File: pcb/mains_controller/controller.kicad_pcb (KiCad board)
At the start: 2 copper layers, 60 x 70 mm, 39 parts, among them J1 Conn_01x03, J2 Conn_01x03, J3 RELAY_CONN, J4 Remote_header, J5 PWR_IN, J6 MFRC_CONN, J7 Micro_SD_Card, J8 Conn_01x03, J9 Conn_01x03, Q1 MMBT3906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

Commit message: Start design for mains controller
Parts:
- removed J3: RELAY_CONN, TerminalBlock_MetzConnect:TerminalBlock_MetzConnect_Type059_RT06302HBWC_1x02_P3.50mm_Horizontal
- removed J4: Remote_header, TerminalBlock_MetzConnect:TerminalBlock_MetzConnect_Type059_RT06304HBWC_1x04_P3.50mm_Horizontal
- removed J5: PWR_IN, TerminalBlock_MetzConnect:TerminalBlock_MetzConnect_Type059_RT06302HBWC_1x02_P3.50mm_Horizontal
- removed JP1: RELAY_VOLT_SELECT, Jumper:SolderJumper-3_P1.3mm_Open_Pad1.0x1.5mm
- removed JP2, JP3: Jumper_2_Open, Jumper:SolderJumper-2_P1.3mm_Open_Pad1.0x1.5mm
- removed Q1, Q2: MMBT3906, Package_TO_SOT_SMD:SOT-23
- removed R1: 5R1, Resistor_SMD:R_1210_3225Metric_Pad1.30x2.65mm_HandSolder
- removed R2: 470R, Resistor_SMD:R_1210_3225Metric_Pad1.30x2.65mm_HandSolder
- removed R8: R10K, Resistor_SMD:R_1210_3225Metric_Pad1.30x2.65mm_HandSolder
- removed U1: ~, RS485_to_ttl:RS485_to_ttl
- removed U2: ~, DC-DC:hw-1338
- added PS1: HLK-PM01, Converter_ACDC:Converter_ACDC_Hi-Link_HLK-PMxx, F.Cu at (53.0, 92.3)
- moved J9 42.5 mm to (35.1, 67.8)
- moved J8 25.8 mm to (35.1, 58.4)
- moved D1 11.5 mm to (59.9, 64.9)
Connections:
- A1 pad 39: +5V -> RELAY+
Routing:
- net +5V: track 110.2 -> 0.00 mm, vias 4 -> 0
- net +3V3: track 208.8 -> 120.9 mm
- net GPIO_ACC4: track 91.6 -> 13.2 mm
- net +VDC: track 55.6 -> 0.00 mm, vias 1 -> 0
- net RS485_RX: track 55.6 -> 15.8 mm
- net GPIO_ACC3: track 45.0 -> 6.91 mm
- net RS485_TX: track 58.8 -> 23.9 mm
- net RELAY-: track 34.6 -> 6.30 mm
- net REMOTE_PWR: track 22.4 -> 0.00 mm, vias 1 -> 0
- net Net-(Q1-B): track 14.2 -> 0.00 mm
- net RELAY+: track 37.9 -> 23.8 mm, vias 0 -> 1
- net GPIO_ACC1: track 66.1 -> 52.1 mm
- net A+: track 10.6 -> 0.00 mm
- net B-: track 10.3 -> 0.00 mm
- net Net-(Q1-C): track 9.68 -> 0.00 mm
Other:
- board text added: "GP4"
- board text removed: "+"
- board text removed: "+5V"
- board text removed: "5V"
- board text removed: "A+"
- board text removed: "B-"
- board text removed: "DC IN"
- board text removed: "DC_IN"
- board text removed: "For 3/5V I/P, bridge JP3 For 7-28VDC I/P, install MP1584 module here"
- board text removed: "Optional RS485 module here"
- board text removed: "PSU for remote unit (optional)"
- board text removed: "Pwr via Remote"
- board text removed: "RELAY"
- board text removed: "Relay pwr"

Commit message: Production version (sent to JLC!)
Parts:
- removed J9: Conn_01x03, Connector_JST:JST_XH_B3B-XH-A_1x03_P2.50mm_Vertical
- added F1: Fuse, Fuse:Fuseholder_Clip-5x20mm_Keystone_3517_Inline_P23.11x6.76mm_D1.70mm_Horizontal, F.Cu at (33.3, 112.8)
- added F2: Fuse, Resistor_THT:R_Axial_DIN0204_L3.6mm_D1.6mm_P5.08mm_Horizontal, F.Cu at (72.5, 104.8)
- added J3: Conn_01x03, TerminalBlock_MetzConnect:TerminalBlock_MetzConnect_Type073_RT02603HBLU_1x03_P5.08mm_Horizontal, F.Cu at (47.4, 125.9)
- added J4: Conn_01x04_Pin, Connector_JST:JST_XH_B4B-XH-A_1x04_P2.50mm_Vertical, F.Cu at (36.0, 57.6)
- added J4: Conn_01x03, TerminalBlock_MetzConnect:TerminalBlock_MetzConnect_Type073_RT02603HBLU_1x03_P5.08mm_Horizontal, F.Cu at (65.6, 126.2)
- added J5: Conn_01x02_Pin, Connector_JST:JST_XH_B2B-XH-A_1x02_P2.50mm_Vertical, F.Cu at (85.5, 58.2)
- added K2: Relay_SPDT, Relay_THT:Relay_SPDT_Omron_G2RL-1-E, F.Cu at (80.5, 88.2)
- added R1: 4k7, Resistor_SMD:R_1210_3225Metric_Pad1.30x2.65mm_HandSolder, F.Cu at (42.0, 63.5)
- added R2: 4k7, Resistor_SMD:R_1210_3225Metric_Pad1.30x2.65mm_HandSolder, F.Cu at (46.0, 63.4)
- added RV1: Varistor, Varistor:RV_Disc_D7mm_W4.9mm_P5mm, F.Cu at (75.1, 96.4)
- J8: value Conn_01x03 -> Conn_01x02_Pin; footprint Connector_JST:JST_XH_B3B-XH-A_1x03_P2.50mm_Vertical -> Connector_JST:JST_XH_B2B-XH-A_1x02_P2.50mm_Vertical
- Q3, R3, R7: moved to F.Cu
- moved J8 52.7 mm to (85.5, 73.4)
- moved REF** 45.0 mm to (36.2, 128.2)
- moved REF** 45.0 mm to (86.2, 128.2)
- moved D1 29.5 mm to (84.1, 81.8)
- moved Q3 21.2 mm to (64.4, 78.7)
- moved R3 19.8 mm to (57.9, 80.8), turned to -90 degrees
- moved R7 19.3 mm to (57.9, 75.3)
- moved D4 13.9 mm to (87.9, 64.4), turned to 180 degrees
- moved PS1 13.3 mm to (64.2, 99.5), turned to 180 degrees
- moved D3 8.90 mm to (87.9, 68.3)
- moved R6 8.57 mm to (81.8, 64.4), turned to 0 degrees
- moved R5 6.76 mm to (81.8, 68.3), turned to 0 degrees
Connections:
- A1 pad 1: RS485_TX -> I2C0_SDA
- A1 pad 2: RS485_RX -> I2C0_SCL
- J8 pad 1: +3V3 -> ACCESS_GRANTED
- J8 pad 2: GPIO_ACC3 -> GND
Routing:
- net LINE: track 0.00 -> 129.9 mm
- net NEUT: track 0.00 -> 113.3 mm
- net RELAY+: track 23.8 -> 117.7 mm
- net I2C0_SCL: track 0.00 -> 38.5 mm
- net Net-(F1-Pad2): track 0.00 -> 37.3 mm
- net RELAY-: track 6.30 -> 39.0 mm
- net SW_LINE: track 0.00 -> 30.3 mm
- net I2C0_SDA: track 0.00 -> 26.7 mm
- net Earth: track 0.00 -> 25.1 mm
- net RS485_TX: track 23.9 -> 0.00 mm
- net MOSFET_GATE: track 17.4 -> 36.2 mm, vias 1 -> 2
- net RS485_RX: track 15.8 -> 0.00 mm
- net GPIO_ACC1: track 52.1 -> 66.2 mm, vias 4 -> 2
- net GPIO_ACC4: track 13.2 -> 0.30 mm, vias 1 -> 0
- net +3V3: track 120.9 -> 132.2 mm, vias 2 -> 1
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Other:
- board size 60 x 70 mm -> 60 x 115 mm
- board text added: "+"
- board text added: "+3v3 GND SDA SCL"
- board text added: "Access Control Gen2 240V Controller V1.1"
- board text added: "DENY"
- board text added: "I2C0"
- board text added: "IN"
- board text added: "L N E"
- board text added: "OK"
- board text added: "OUT"
- board text removed: "Access Control Gen2 LowVolt Controller V1.1"
- board text removed: "GP4"
- board text removed: "Relay Mosfet"
- board text removed: "Vin"

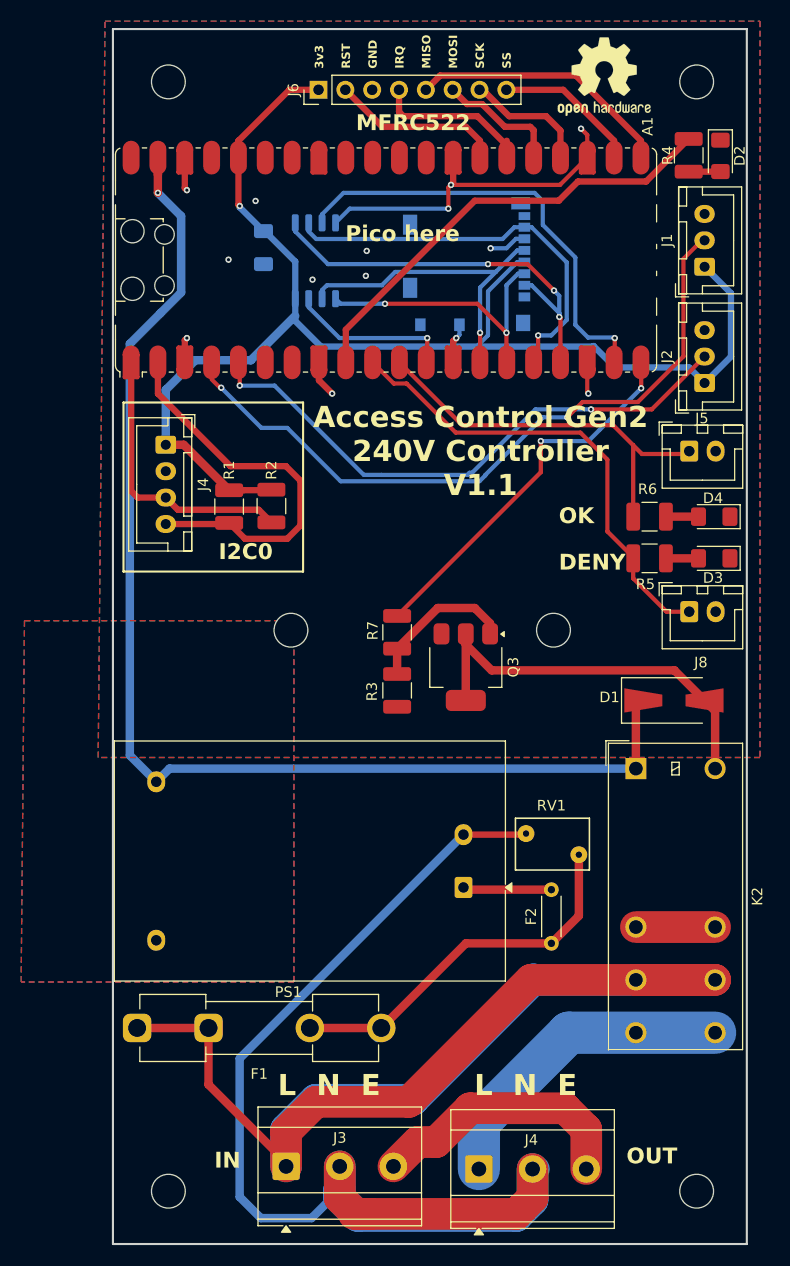
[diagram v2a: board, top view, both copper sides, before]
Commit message: Reposition securing holes for mfrc522 Make hole sizes bigger for varistor and thermal fuse Bump ver to 1.3
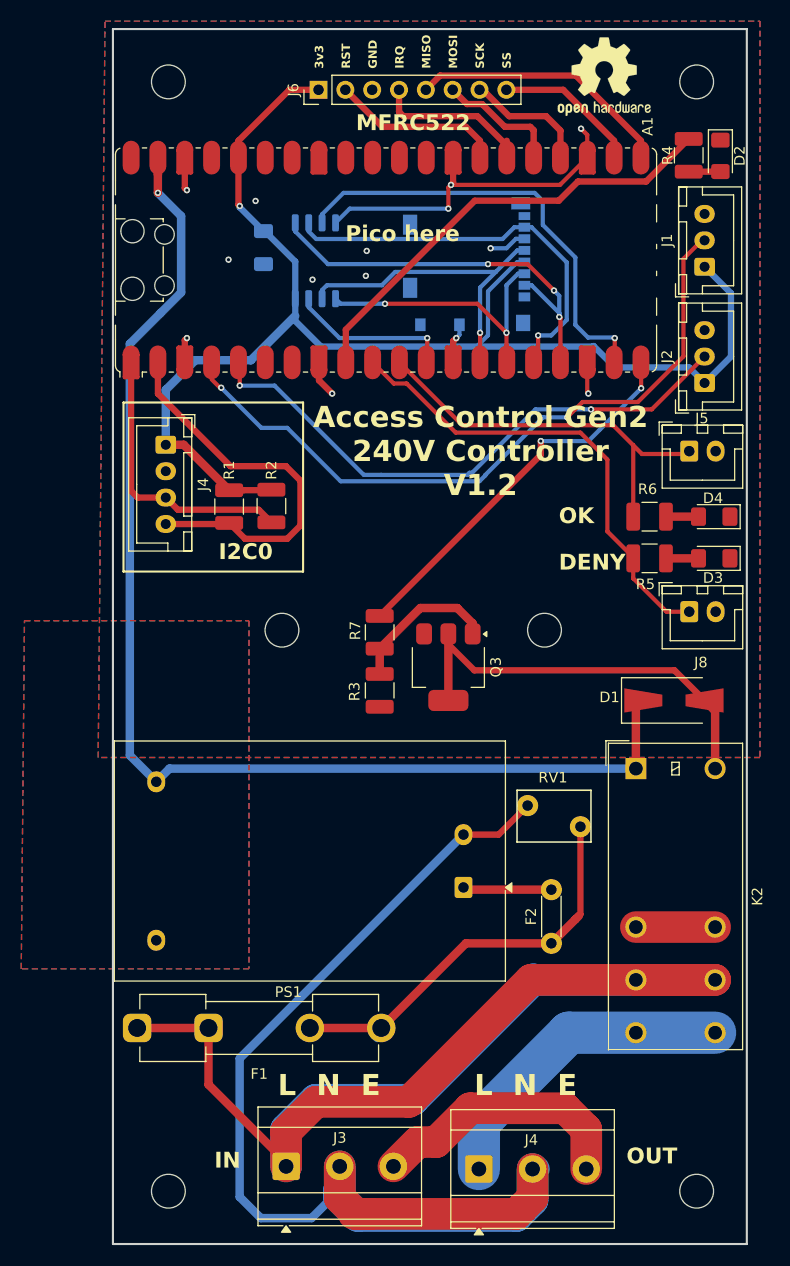
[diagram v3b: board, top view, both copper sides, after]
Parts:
- moved RV1 2.65 mm to (75.2, 93.8)
- moved Q3 1.65 mm to (62.8, 78.7)
- moved R3 1.65 mm to (56.2, 80.8)
- moved R7 1.65 mm to (56.2, 75.3)
- moved REF** 0.85 mm to (71.8, 75.2)
- moved REF** 0.85 mm to (47.0, 75.2)
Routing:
- net Net-(F1-Pad2): track 37.3 -> 40.5 mm
- net RELAY-: track 39.0 -> 40.6 mm
- net NEUT: track 113.3 -> 114.6 mm
- net MOSFET_GATE: track 36.2 -> 36.9 mm
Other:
- board text added: "Access Control Gen2 240V Controller V1.2"
- board text removed: "Access Control Gen2 240V Controller V1.1"
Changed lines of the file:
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@@
 	(footprint "Package_TO_SOT_SMD:SOT-223-3_TabPin2"
 		(layer "F.Cu")
-		(at 64.4 78.65 -90)
+		(at 62.75 78.65 -90)
 		(descr "module CMS SOT223 4 pins")
 		(tags "CMS SOT")
@@
 		(pad "1" thru_hole circle
 			(at 0 0 90)
-			(size 1.4 1.4)
-			(drill 0.7)
+			(size 2 2)
+			(drill 1)
 			(layers "*.Cu" "*.Mask")
 			(remove_unused_layers no)
@@
 		(pad "2" thru_hole circle
 			(at 5.08 0 90)
-			(size 1.4 1.4)
-			(drill 0.7)
+			(size 2 2)
+			(drill 1)
 			(layers "*.Cu" "*.Mask")
 			(remove_unused_layers no)
@@
 	(footprint "Resistor_SMD:R_1210_3225Metric_Pad1.30x2.65mm_HandSolder"
 		(layer "F.Cu")
-		(at 57.9 75.35 -90)
+		(at 56.25 75.35 -90)
 		(descr "Resistor SMD 1210 (3225 Metric), square (rectangular) end terminal, IPC-7351 nominal with elongated pad for handsoldering. (Body size source: IPC-SM-782 page 72, https://www.pcb-3d.com/wordpress/wp-content/uploads/ipc-sm-782a_amendment_1_and_2.pdf), generated with kicad-footprint-generator")
 		(tags "resistor handsolder")
@@
 	(footprint "Resistor_SMD:R_1210_3225Metric_Pad1.30x2.65mm_HandSolder"
 		(layer "F.Cu")
-		(at 57.9 80.85 -90)
+		(at 56.25 80.85 -90)
 		(descr "Resistor SMD 1210 (3225 Metric), square (rectangular) end terminal, IPC-7351 nominal with elongated pad for handsoldering. (Body size source: IPC-SM-782 page 72, https://www.pcb-3d.com/wordpress/wp-content/uploads/ipc-sm-782a_amendment_1_and_2.pdf), generated with kicad-footprint-generator")
 		(tags "resistor handsolder")
@@
 	(footprint "Varistor:RV_Disc_D7mm_W4.9mm_P5mm"
 		(layer "F.Cu")
-		(at 75.1 96.4 180)
+		(at 75.25 93.75 180)
 		(descr "Varistor, diameter 7mm, width 4.9mm, pitch 5mm")
 		(tags "varistor SIOV")
@@
 		(pad "1" thru_hole circle
 			(at 0 0 180)
-			(size 1.6 1.6)
-			(drill 0.6)
+			(size 2 2)
+			(drill 1)
 			(layers "*.Cu" "*.Mask")
 			(remove_unused_layers no)
@@
 		(pad "2" thru_hole circle
 			(at 5 2 180)
-			(size 1.6 1.6)
-			(drill 0.6)
+			(size 2 2)
+			(drill 1)
 			(layers "*.Cu" "*.Mask")
 			(remove_unused_layers no)
@@
 	(footprint "MountingHole:MountingHole_3.2mm_M3"
 		(layer "F.Cu")
-		(at 47.85 75.15)
+		(at 47 75.15)
 		(descr "Mounting Hole 3.2mm, no annular, M3")
 		(tags "mounting hole 3.2mm no annular m3")
@@
 	(footprint "MountingHole:MountingHole_3.2mm_M3"
 		(layer "F.Cu")
-		(at 72.7 75.15)
+		(at 71.85 75.15)
 		(descr "Mounting Hole 3.2mm, no annular, M3")
 		(tags "mounting hole 3.2mm no annular m3")
@@
 		)
 	)
-	(gr_text "Access Control Gen2\n240V Controller\nV1.1"
+	(gr_text "Access Control Gen2\n240V Controller\nV1.2"
 		(at 65.8 62.6 0)
 		(layer "F.SilkS")
@@
 	)
 	(segment
-		(start 71.5 60.2)
+		(start 71.5 58.55)
 		(end 71.5 57.25)
-		(width 0.4)
+		(width 0.6)
 		(layer "F.Cu")
 		(net 30)
 	)
 	(segment
-		(start 57.9 73.8)
-		(end 71.5 60.2)
-		(width 0.4)
+		(start 56.25 73.8)
+		(end 71.5 58.55)
+		(width 0.6)
 		(layer "F.Cu")
 		(net 30)
@@
 	)
 	(segment
-		(start 88 88.25)
-		(end 88 82.8)
-		(width 0.8)
+		(start 62.75 76.5)
+		(end 62.75 75.5)
+		(width 0.6)
 		(layer "F.Cu")
 		(net 33)
 	)
 	(segment
-		(start 88 82.8)
-		(end 87 81.8)
+		(start 88 88.25)
+		(end 88 82.8)
 		(width 0.8)
 		(layer "F.Cu")
@@
 	)
 	(segment
-		(start 87 81.8)
-		(end 84.15 78.95)
-		(width 0.8)
+		(start 84.15 78.95)
+		(end 65.2 78.95)
+		(width 0.6)
 		(layer "F.Cu")
 		(net 33)
 	)
 	(segment
-		(start 64.4 76.5)
-		(end 64.4 75.5)
+		(start 88 82.8)
+		(end 87 81.8)
 		(width 0.8)
 		(layer "F.Cu")
@@
 	)
 	(segment
-		(start 84.15 78.95)
-		(end 66.85 78.95)
+		(start 62.75 81.8)
+		(end 62.75 75.5)
 		(width 0.8)
 		(layer "F.Cu")
@@
 	)
 	(segment
-		(start 64.4 81.8)
-		(end 64.4 75.5)
-		(width 0.8)
+		(start 65.2 78.95)
+		(end 62.75 76.5)
+		(width 0.6)
 		(layer "F.Cu")
 		(net 33)
 	)
 	(segment
-		(start 66.85 78.95)
-		(end 64.4 76.5)
-		(width 0.8)
+		(start 87 81.8)
+		(end 84.15 78.95)
+		(width 0.6)
 		(layer "F.Cu")
 		(net 33)
@@
 	)
 	(segment
-		(start 66.7 74.5)
-		(end 66.7 75.5)
+		(start 65.05 74.5)
+		(end 65.05 75.5)
 		(width 0.8)
 		(layer "F.Cu")
@@
 	)
 	(segment
-		(start 61.75 73.05)
-		(end 65.25 73.05)
+		(start 60.1 73.05)
+		(end 63.6 73.05)
 		(width 0.8)
 		(layer "F.Cu")
@@
 	)
 	(segment
-		(start 57.9 76.9)
-		(end 61.75 73.05)
+		(start 56.25 76.9)
+		(end 60.1 73.05)
 		(width 0.8)
 		(layer "F.Cu")
@@
 	)
 	(segment
-		(start 57.9 79.3)
-		(end 57.9 76.9)
+		(start 56.25 79.3)
+		(end 56.25 76.9)
 		(width 0.8)
 		(layer "F.Cu")
@@
 	)
 	(segment
-		(start 65.25 73.05)
-		(end 66.7 74.5)
+		(start 63.6 73.05)
+		(end 65.05 74.5)
 		(width 0.8)
 		(layer "F.Cu")
@@
 	)
 	(segment
-		(start 70 94.5)
-		(end 70.1 94.4)
+		(start 70.25 91.75)
+		(end 67.5 94.5)
+		(width 0.6)
+		(layer "F.Cu")
+		(net 42)
+	)
+	(segment
+		(start 67.5 94.5)
+		(end 64.18 94.5)
 		(width 0.6)
 		(layer "F.Cu")
@@
 	)
 	(segment
-		(start 64.18 94.5)
-		(end 70 94.5)
-		(width 0.6)
-		(layer "F.Cu")
-		(net 42)
-	)
-	(segment
 		(start 69.8 129.8)
 		(end 69.2 130.4)
@@
 	)
 	(segment
-		(start 75.1 102.19)
+		(start 75.25 93.75)
+		(end 75.25 102.04)
+		(width 0.6)
+		(layer "F.Cu")
+		(net 48)
+	)
+	(segment
+		(start 75.25 102.04)
+		(end 74.77 102.52)
+		(width 0.6)
+		(layer "F.Cu")
+		(net 48)
+	)
+	(segment
+		(start 74.77 102.52)
 		(end 72.5 104.79)
 		(width 0.8)
@@
 	)
 	(segment
-		(start 75.1 96.4)
-		(end 75.1 102.19)
+		(start 72.5 104.79)
+		(end 64.41 104.79)
 		(width 0.8)
 		(layer "F.Cu")
@@
 	)
 	(segment
-		(start 72.5 104.79)
-		(end 64.41 104.79)
+		(start 75.1 102.19)
+		(end 74.77 102.52)
 		(width 0.8)
 		(layer "F.Cu")
@@
 		(min_thickness 0.25)
 		(filled_areas_thickness no)
-		(fill yes
+		(fill
 			(thermal_gap 0.5)
 			(thermal_bridge_width 0.5)
@@
 		(polygon
 			(pts
-				(xy 22.627313 74.25) (xy 48.129629 74.25) (xy 48.129629 108.45) (xy 22.310646 108.45)
+				(xy 22.627313 74.25) (xy 43.879629 74.25) (xy 43.879629 107.2) (xy 22.32222 107.2)
 			)
 		)
